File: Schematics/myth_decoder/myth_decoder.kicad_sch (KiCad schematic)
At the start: 8 parts, among them U1 74HC74, U2 74LS08, U3 74LS32, U4 74HC157, U5 74HC157, U6 74AHC273, U7 74LS148, U8 74AHC138

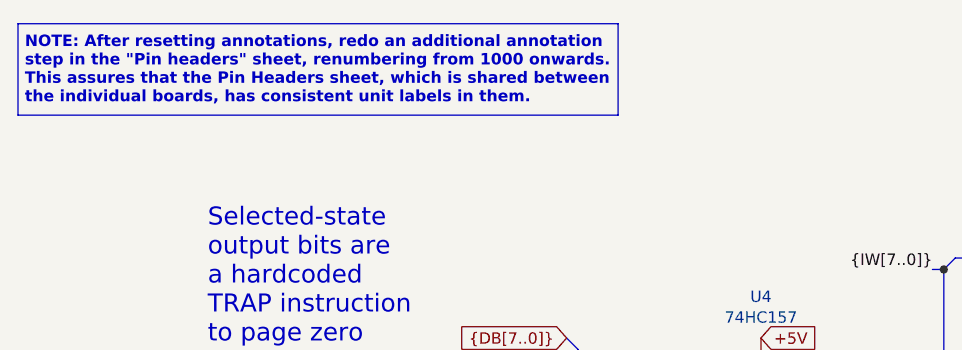
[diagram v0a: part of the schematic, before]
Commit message: Reduce number of shared headers
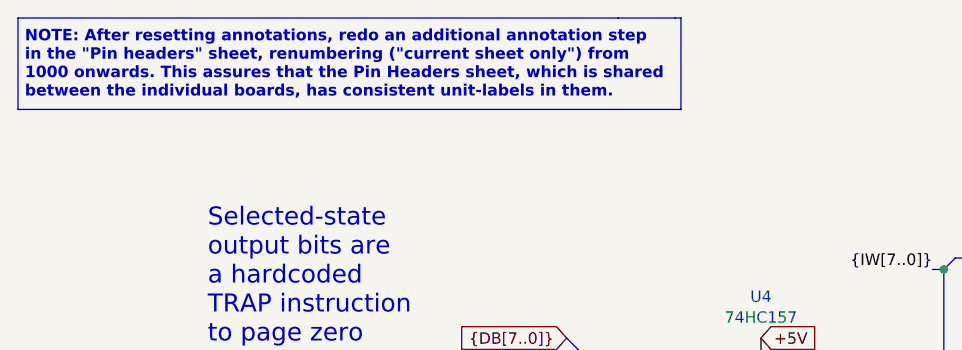
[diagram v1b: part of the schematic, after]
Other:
- note added: "NOTE: After resetting annotations, redo an additional annotation step in the "Pin headers" sheet, renumbering ("current sheet only") from 1000 onwards. This assures that the Pin Headers sheet, which is shared between the individual boards, has consistent unit-labels in them."
- note removed: "NOTE: After resetting annotations, redo an additional annotation step in the "Pin headers" sheet, renumbering from 1000 onwards. This assures that the Pin Headers sheet, which is shared between the individual boards, has consistent unit labels in them."

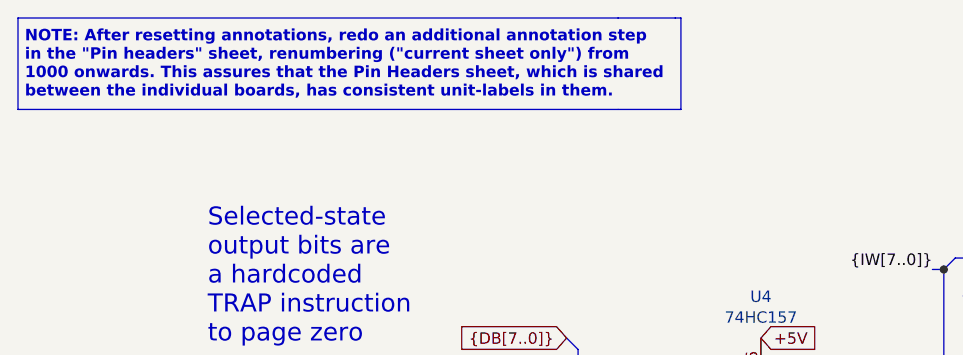
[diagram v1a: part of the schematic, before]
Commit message: Improve schematics for readability
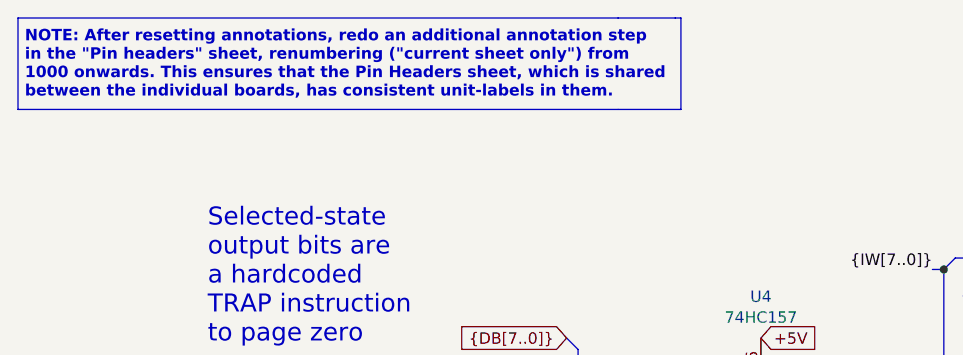
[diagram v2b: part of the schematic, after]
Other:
- note added: "NOTE: After resetting annotations, redo an additional annotation step in the "Pin headers" sheet, renumbering ("current sheet only") from 1000 onwards. This ensures that the Pin Headers sheet, which is shared between the individual boards, has consistent unit-labels in them."
- note removed: "NOTE: After resetting annotations, redo an additional annotation step in the "Pin headers" sheet, renumbering ("current sheet only") from 1000 onwards. This assures that the Pin Headers sheet, which is shared between the individual boards, has consistent unit-labels in them."
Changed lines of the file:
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@@
 		)
 	)
-	(text "NOTE: After resetting annotations, redo an additional annotation step\nin the \"Pin headers\" sheet, renumbering (\"current sheet only\") from\n1000 onwards. This assures that the Pin Headers sheet, which is shared\nbetween the individual boards, has consistent unit-labels in them."
+	(text "NOTE: After resetting annotations, redo an additional annotation step\nin the \"Pin headers\" sheet, renumbering (\"current sheet only\") from\n1000 onwards. This ensures that the Pin Headers sheet, which is shared\nbetween the individual boards, has consistent unit-labels in them."
 		(exclude_from_sim no)
 		(at 14.732 22.987 0)

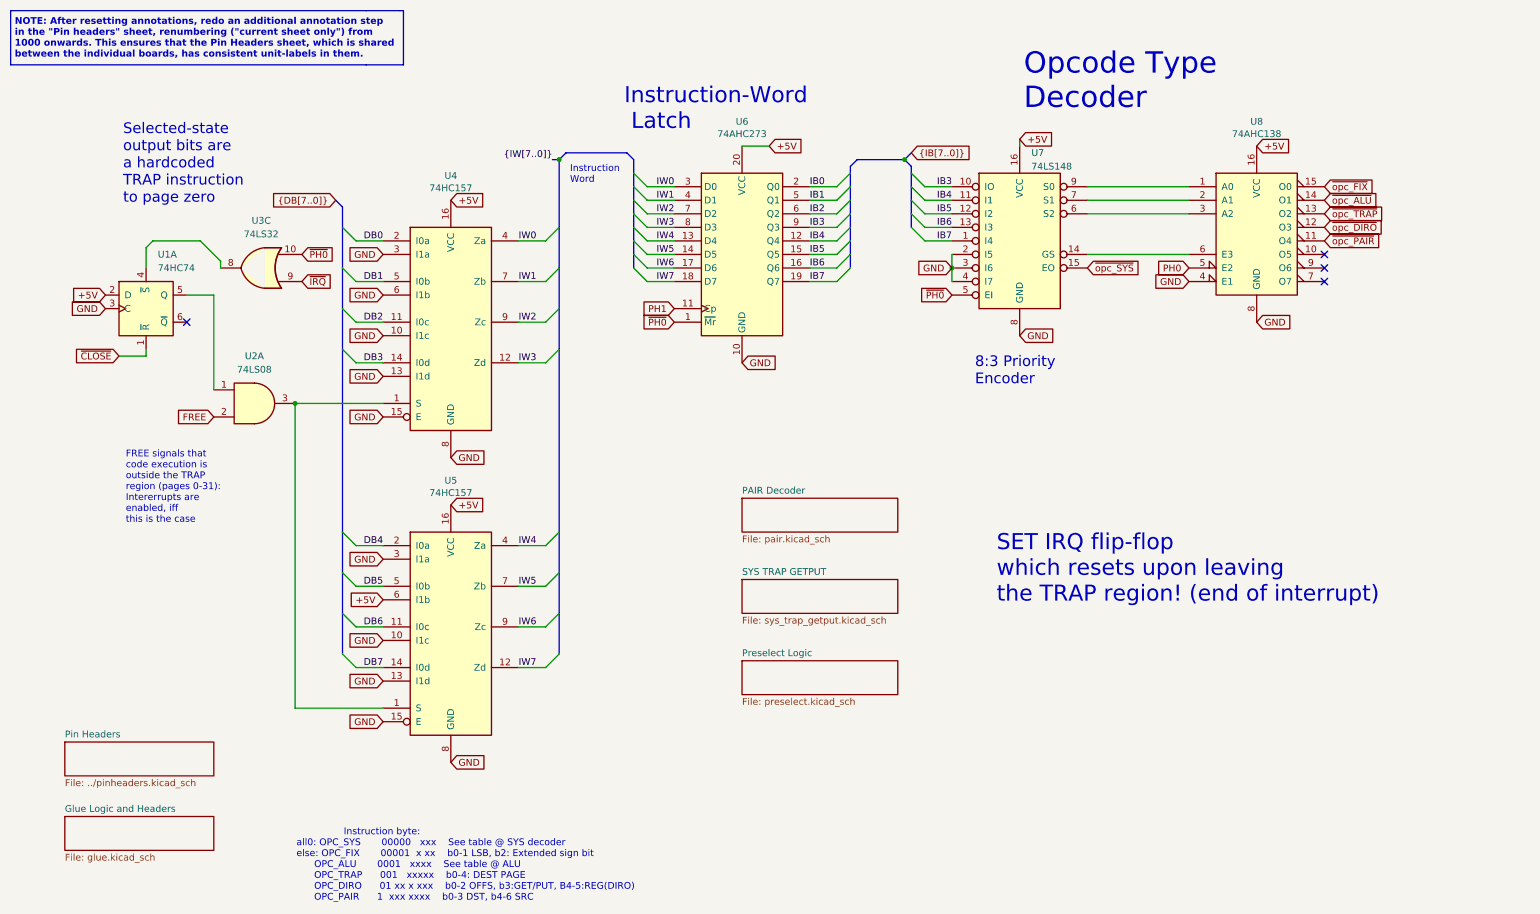
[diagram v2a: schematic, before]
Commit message: Change d to g
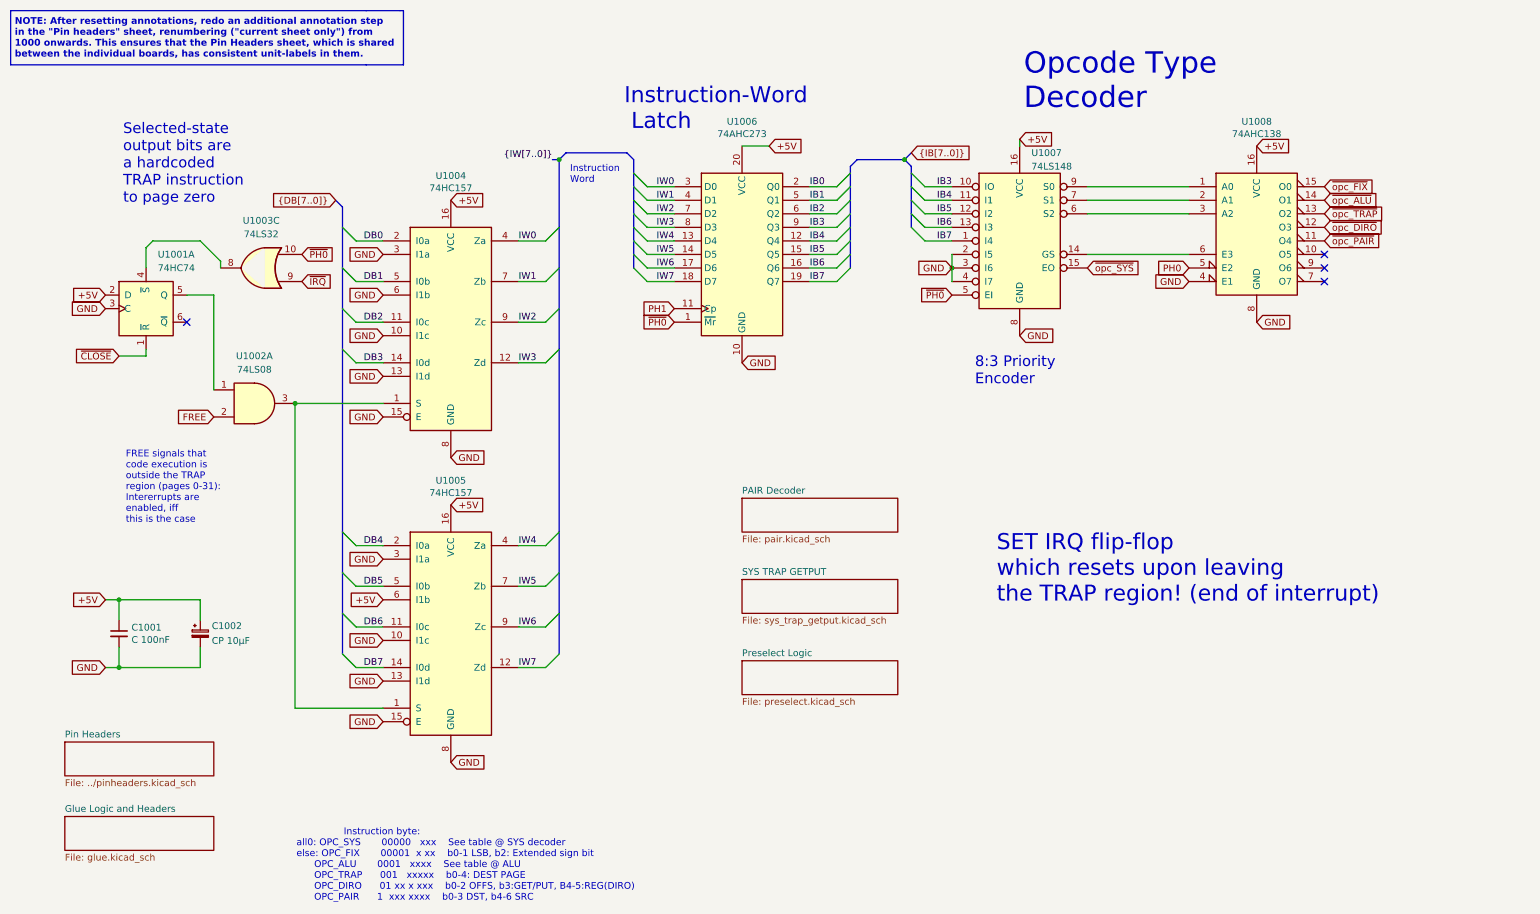
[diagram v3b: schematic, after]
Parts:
- added C1001: C 100nF, Capacitor_THT:C_Disc_D5.0mm_W2.5mm_P2.50mm, symbol Device:C_Small
- added C1002: CP 10μF, Capacitor_THT:CP_Radial_D6.3mm_P2.50mm, symbol Device:C_Polarized_Small
- renumbered U1 to U1001, U2 to U1002, U3 to U1003, U4 to U1004, U5 to U1005, U6 to U1006, U7 to U1007, U8 to U1008
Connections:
- net +5V: now also C1001.1, C1002.1
- net GND: now also C1001.2, C1002.2

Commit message: Change CO do D
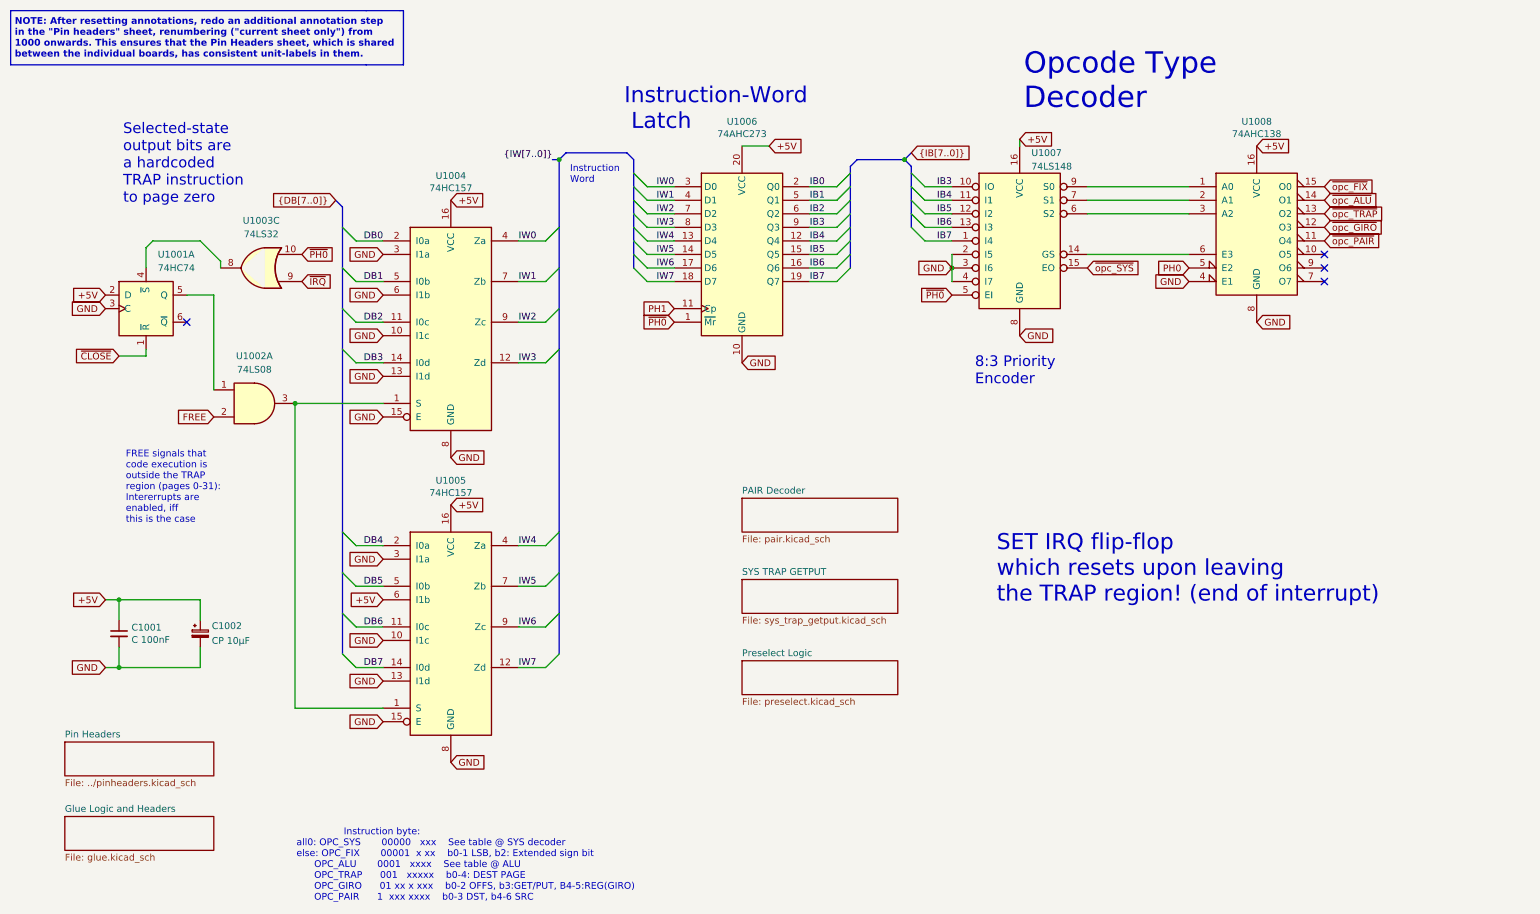
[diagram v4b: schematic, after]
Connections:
- net ~{opc_DIRO} renamed ~{opc_GIRO}
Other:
- note added: "Instruction byte: all0: OPC_SYS 00000 xxx See table @ SYS decoder else: OPC_FIX 00001 x xx b0-1 LSB, b2: Extended sign bit OPC_ALU 0001 xxxx See table @ ALU OPC_TRAP 001 xxxxx b0-4: DEST PAGE OPC_GIRO 01 xx x xxx b0-2 OFFS, b3:GET/PUT, B4-5:REG(GIRO) OPC_PAIR 1 xxx xxxx b0-3 DST, b4-6 SRC"
- note removed: "Instruction byte: all0: OPC_SYS 00000 xxx See table @ SYS decoder else: OPC_FIX 00001 x xx b0-1 LSB, b2: Extended sign bit OPC_ALU 0001 xxxx See table @ ALU OPC_TRAP 001 xxxxx b0-4: DEST PAGE OPC_DIRO 01 xx x xxx b0-2 OFFS, b3:GET/PUT, B4-5:REG(DIRO) OPC_PAIR 1 xxx xxxx b0-3 DST, b4-6 SRC"
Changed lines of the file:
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@@
 		)
 	)
-	(text "                Instruction byte:\nall0: OPC_SYS       00000   xxx    See table @ SYS decoder\nelse: OPC_FIX       00001  x xx    b0-1 LSB, b2: Extended sign bit\n      OPC_ALU       0001   xxxx    See table @ ALU\n      OPC_TRAP      001   xxxxx    b0-4: DEST PAGE\n      OPC_DIRO      01 xx x xxx    b0-2 OFFS, b3:GET/PUT, B4-5:REG(DIRO)\n      OPC_PAIR      1  xxx xxxx    b0-3 DST, b4-6 SRC"
+	(text "                Instruction byte:\nall0: OPC_SYS       00000   xxx    See table @ SYS decoder\nelse: OPC_FIX       00001  x xx    b0-1 LSB, b2: Extended sign bit\n      OPC_ALU       0001   xxxx    See table @ ALU\n      OPC_TRAP      001   xxxxx    b0-4: DEST PAGE\n      OPC_GIRO      01 xx x xxx    b0-2 OFFS, b3:GET/PUT, B4-5:REG(GIRO)\n      OPC_PAIR      1  xxx xxxx    b0-3 DST, b4-6 SRC"
 		(exclude_from_sim no)
 		(at 67.564 181.102 0)
@@
 		)
 	)
-	(global_label "~{opc_DIRO}"
+	(global_label "~{opc_GIRO}"
 		(shape input)
 		(at 260.35 54.61 0)

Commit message: Change semantics of xB
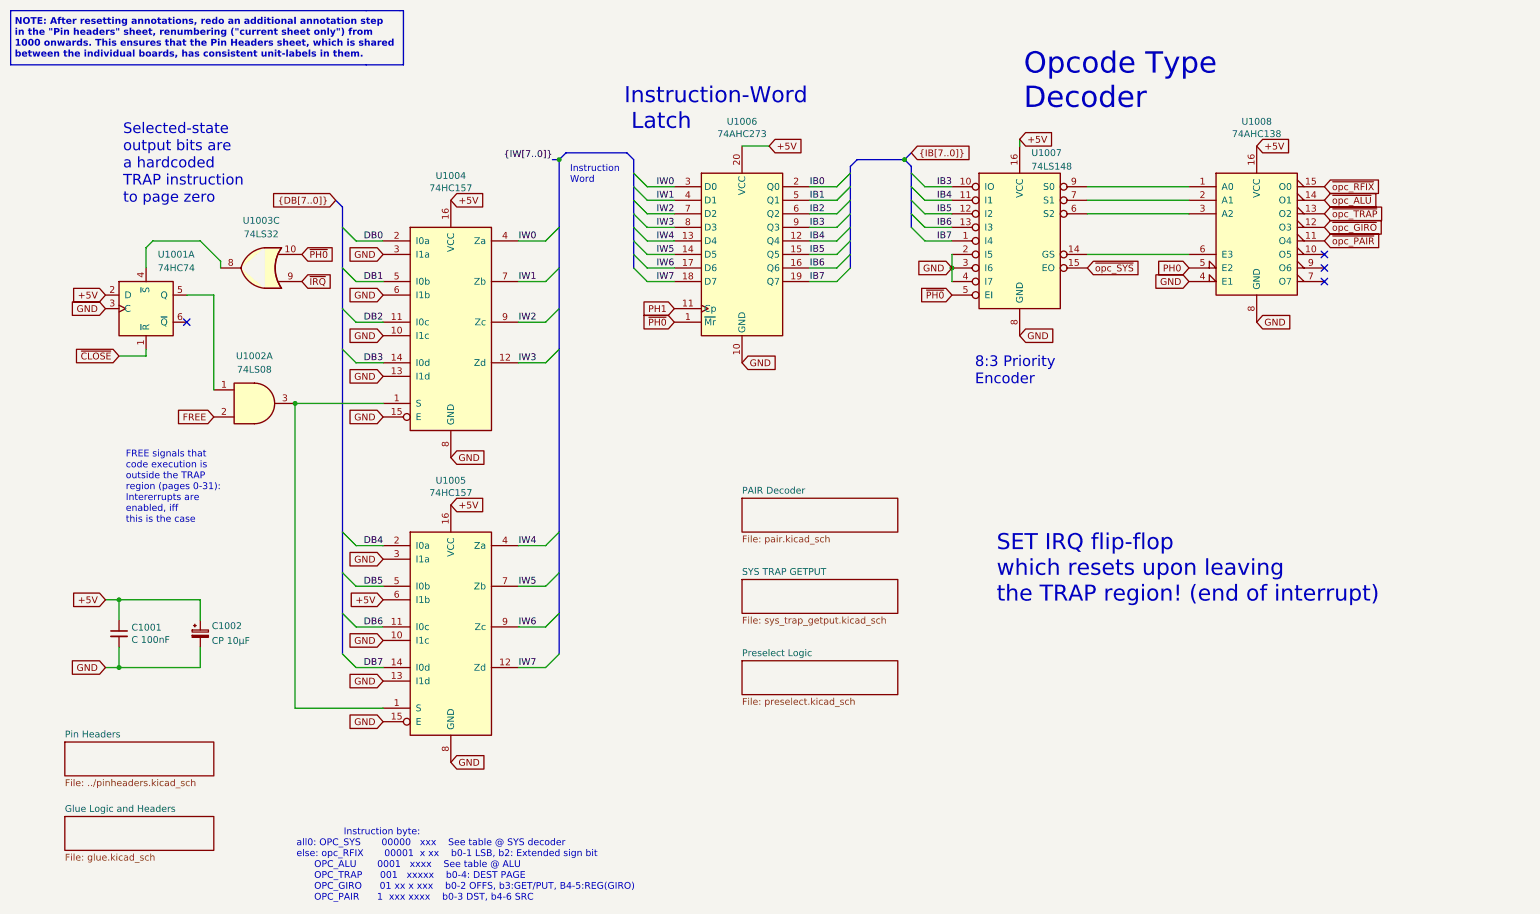
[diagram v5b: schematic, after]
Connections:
- net ~{opc_FIX} renamed ~{opc_RFIX}
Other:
- note added: "Instruction byte: all0: OPC_SYS 00000 xxx See table @ SYS decoder else: opc_RFIX 00001 x xx b0-1 LSB, b2: Extended sign bit OPC_ALU 0001 xxxx See table @ ALU OPC_TRAP 001 xxxxx b0-4: DEST PAGE OPC_GIRO 01 xx x xxx b0-2 OFFS, b3:GET/PUT, B4-5:REG(GIRO) OPC_PAIR 1 xxx xxxx b0-3 DST, b4-6 SRC"
- note removed: "Instruction byte: all0: OPC_SYS 00000 xxx See table @ SYS decoder else: OPC_FIX 00001 x xx b0-1 LSB, b2: Extended sign bit OPC_ALU 0001 xxxx See table @ ALU OPC_TRAP 001 xxxxx b0-4: DEST PAGE OPC_GIRO 01 xx x xxx b0-2 OFFS, b3:GET/PUT, B4-5:REG(GIRO) OPC_PAIR 1 xxx xxxx b0-3 DST, b4-6 SRC"
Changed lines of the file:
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@@
 		)
 	)
-	(text "                Instruction byte:\nall0: OPC_SYS       00000   xxx    See table @ SYS decoder\nelse: OPC_FIX       00001  x xx    b0-1 LSB, b2: Extended sign bit\n      OPC_ALU       0001   xxxx    See table @ ALU\n      OPC_TRAP      001   xxxxx    b0-4: DEST PAGE\n      OPC_GIRO      01 xx x xxx    b0-2 OFFS, b3:GET/PUT, B4-5:REG(GIRO)\n      OPC_PAIR      1  xxx xxxx    b0-3 DST, b4-6 SRC"
+	(text "                Instruction byte:\nall0: OPC_SYS       00000   xxx    See table @ SYS decoder\nelse: opc_RFIX       00001  x xx    b0-1 LSB, b2: Extended sign bit\n      OPC_ALU       0001   xxxx    See table @ ALU\n      OPC_TRAP      001   xxxxx    b0-4: DEST PAGE\n      OPC_GIRO      01 xx x xxx    b0-2 OFFS, b3:GET/PUT, B4-5:REG(GIRO)\n      OPC_PAIR      1  xxx xxxx    b0-3 DST, b4-6 SRC"
 		(exclude_from_sim no)
 		(at 67.564 181.102 0)
@@
 		)
 	)
-	(global_label "~{opc_FIX}"
+	(global_label "~{opc_RFIX}"
 		(shape input)
 		(at 260.35 46.99 0)
